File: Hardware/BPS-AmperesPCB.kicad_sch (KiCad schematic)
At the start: 34 parts, among them IC1 INA241A5IDR, IC2 AMC1350DWVR, IC3 OPA396DCKR, J1 Scrut In, J2 Shunt Resistor, SW1 Scrut Select, U1 TLV6001DCK

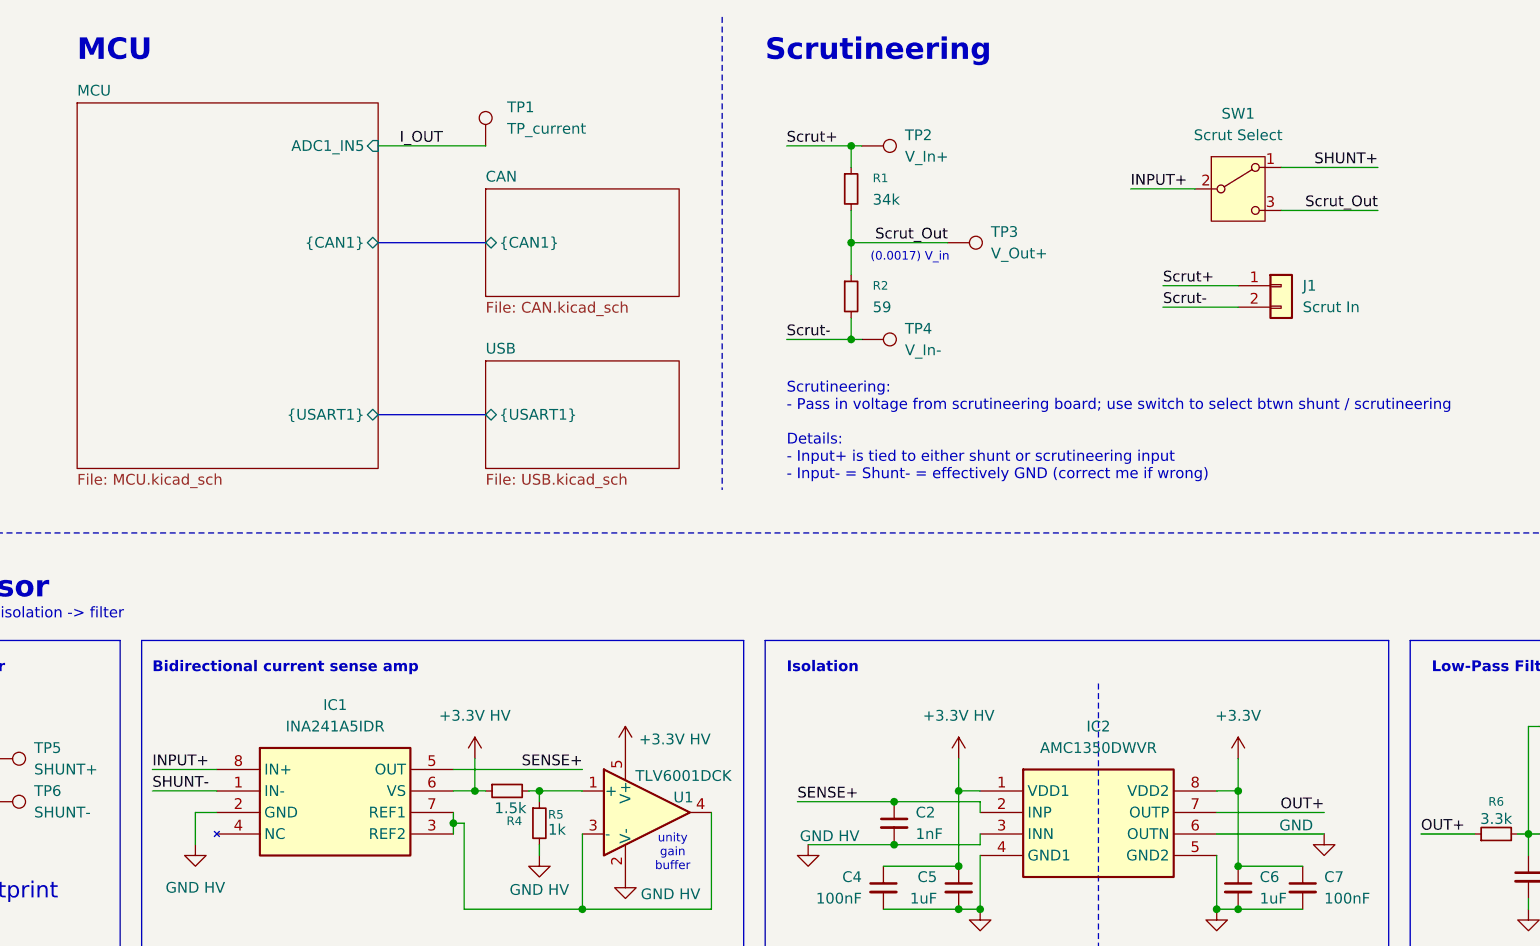
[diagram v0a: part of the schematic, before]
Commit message: dpdt switch for scrutineering
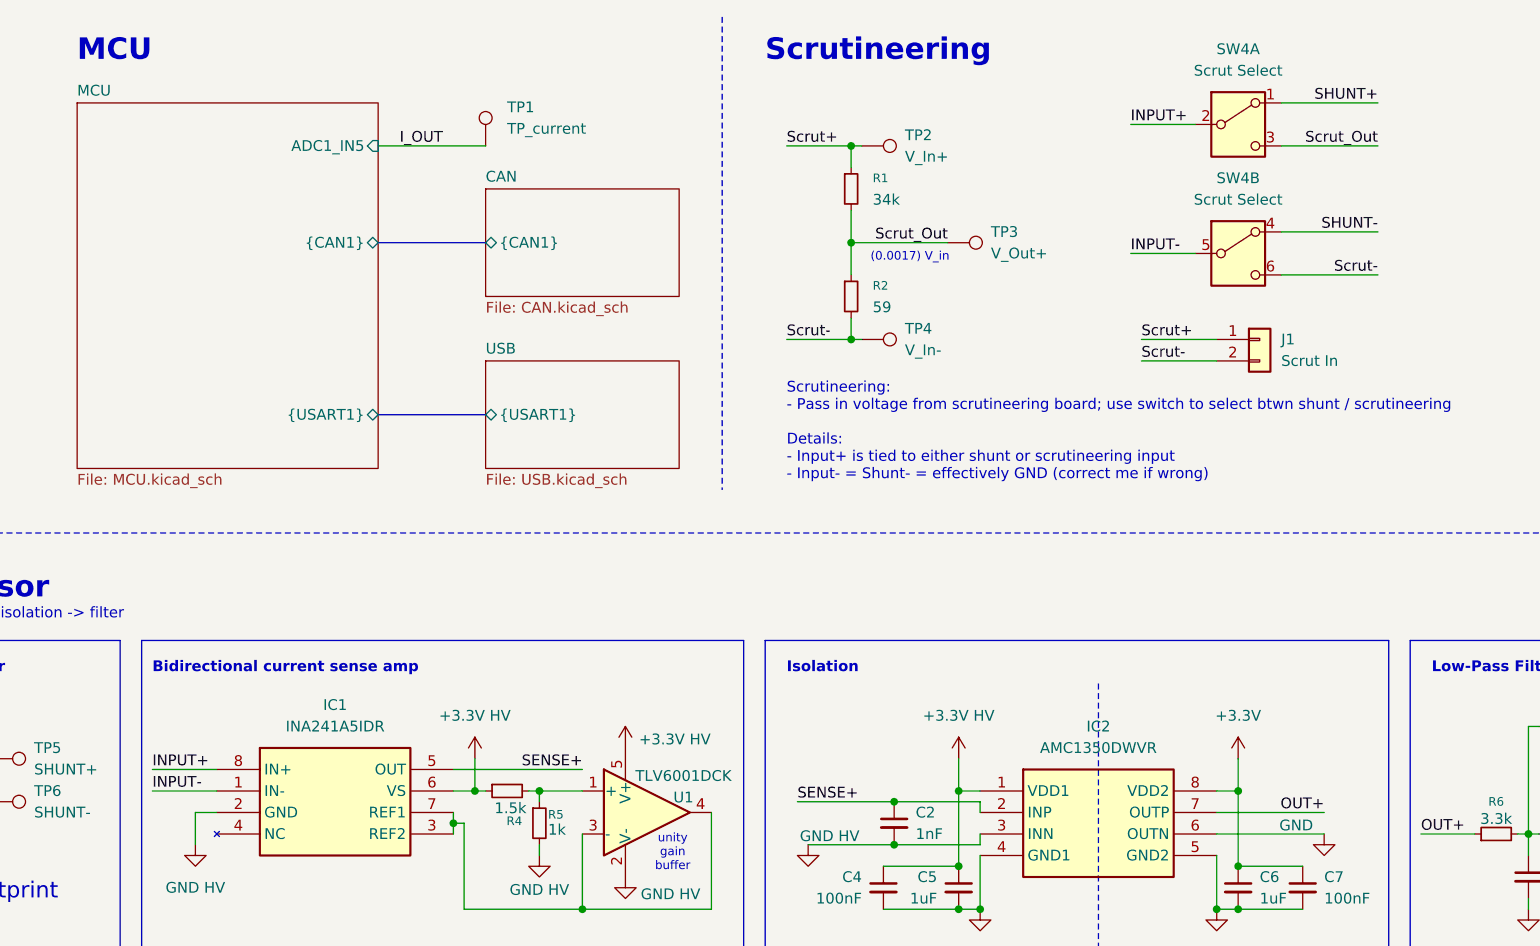
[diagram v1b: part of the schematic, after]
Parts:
- removed SW1: Scrut Select, symbol Switch:SW_SPDT
- added SW4: Scrut Select, symbol Switch:SW_DPDT_x2
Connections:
- net INPUT+: now also SW4.2 (B)
- net SHUNT+: now also SW4.1 (A)
- net SHUNT-: now also SW4.4 (A); no longer IC1.1 (IN-)
- net Scrut-: now also SW4.6 (C)
- net Scrut_Out: now also SW4.3 (C)
- new net INPUT-: IC1.1 (IN-), SW4.5 (B)
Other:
- moved on the sheet: J1

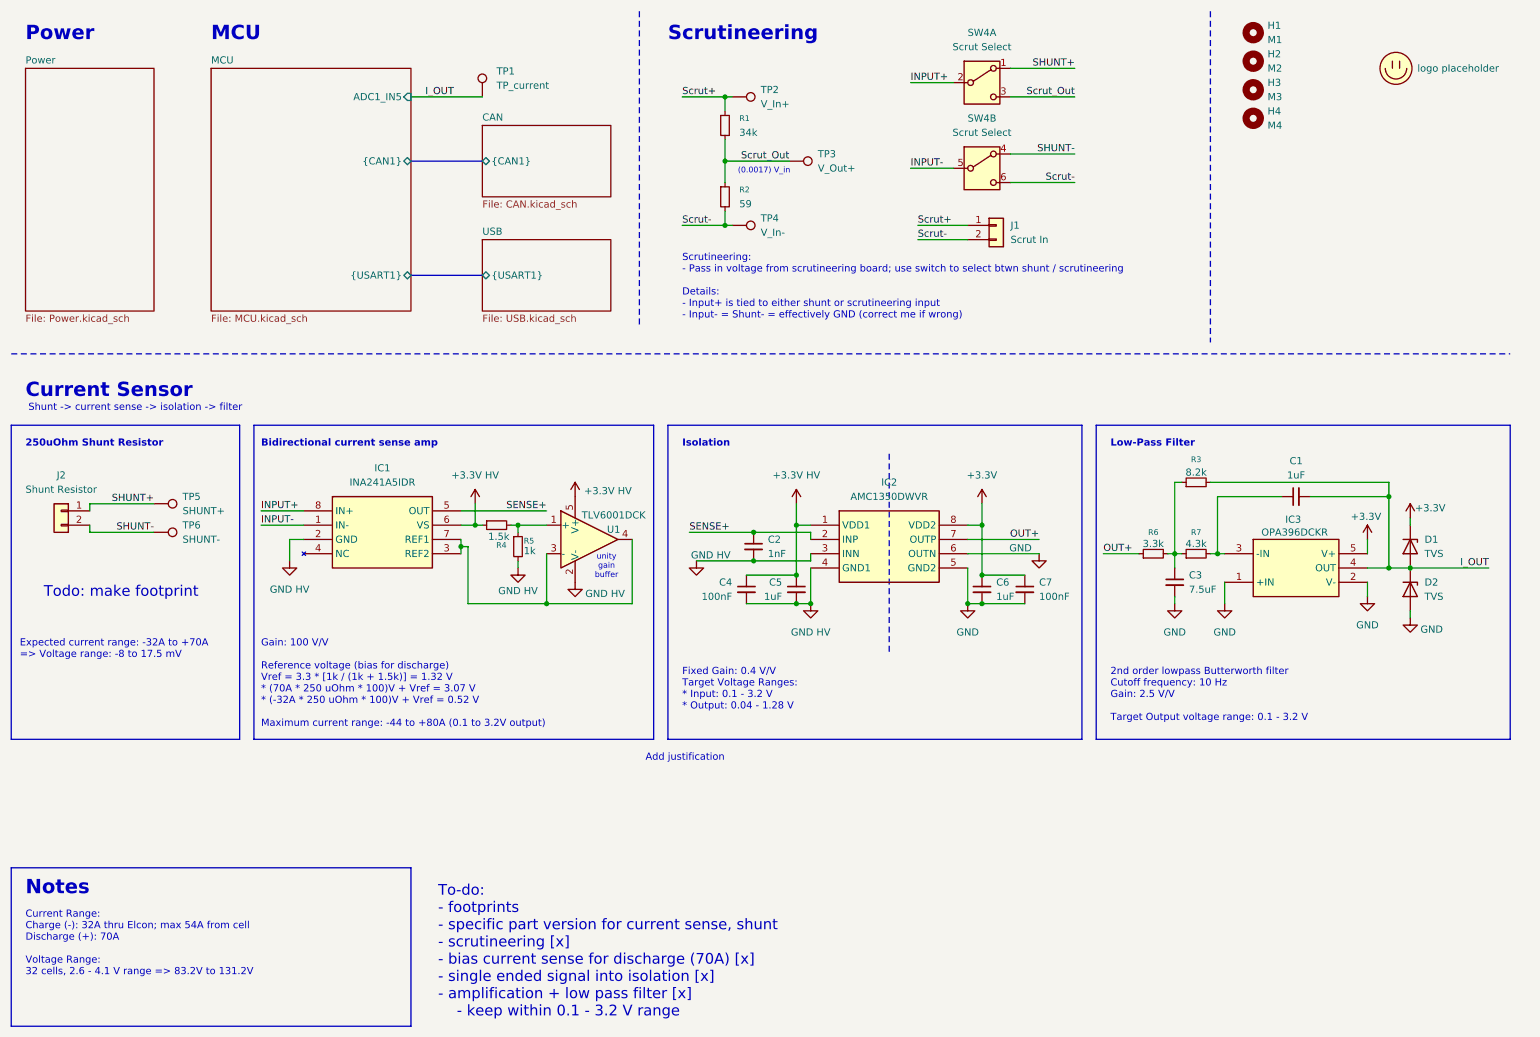
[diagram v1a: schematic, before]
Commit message: 24-5 buck from psom, OR gate for bootload. more sheet organization
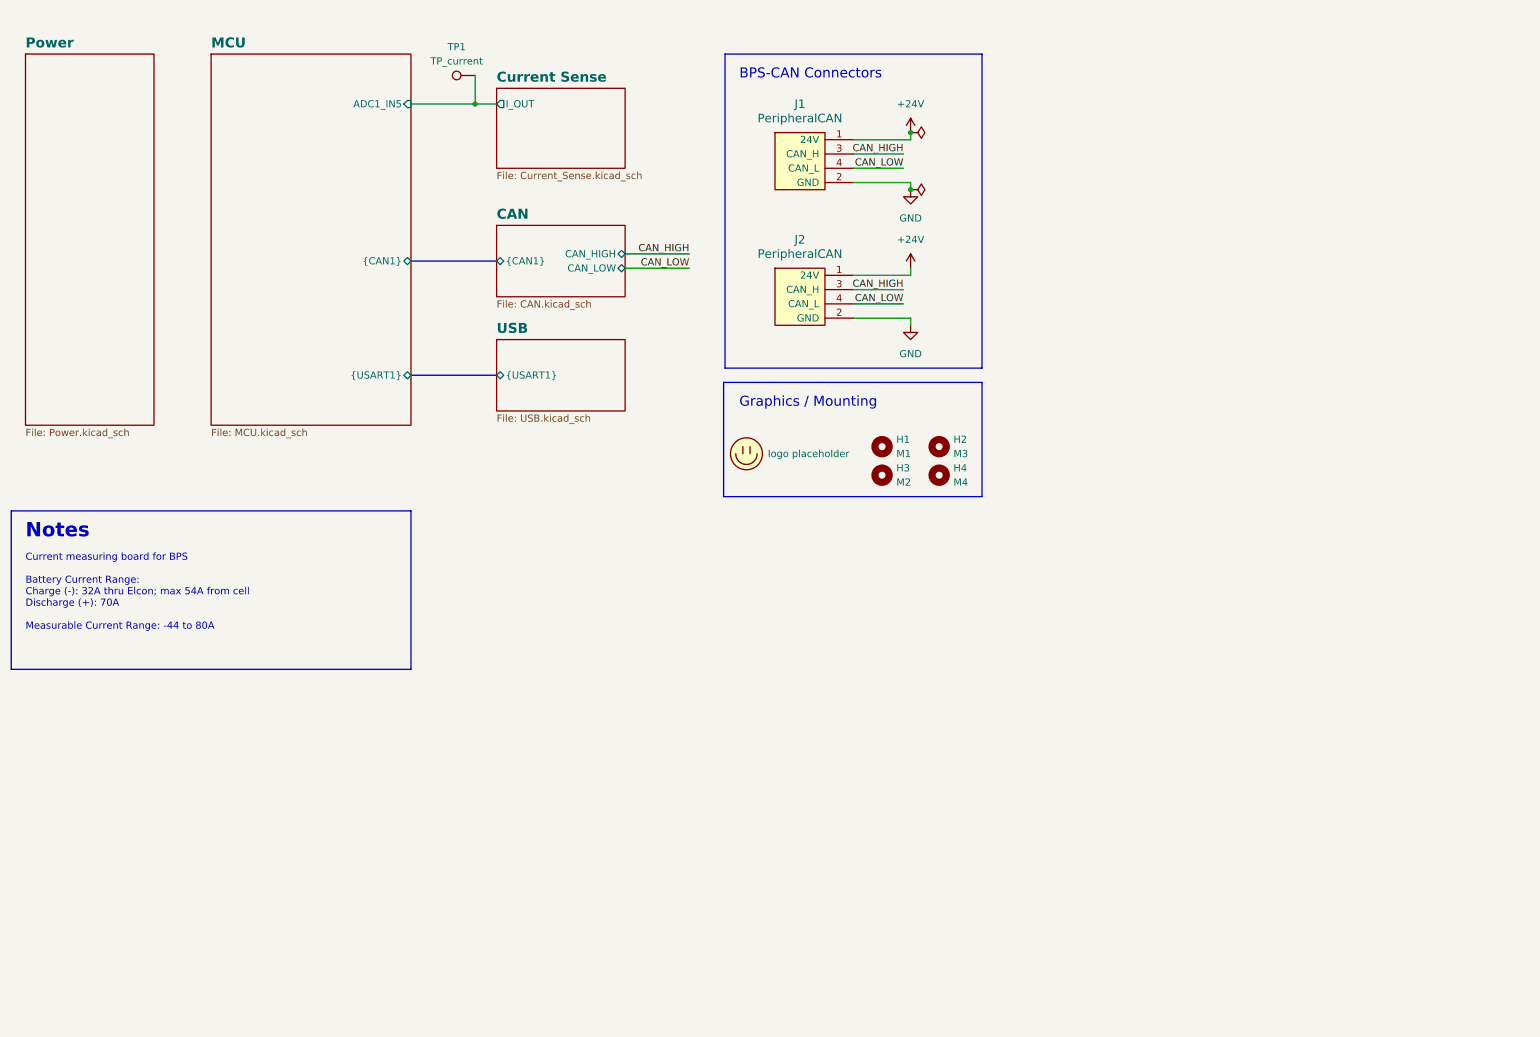
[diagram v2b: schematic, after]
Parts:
- removed C1, C5, C6: 1uF, Capacitor_SMD:C_0603_1608Metric_Pad1.08x0.95mm_HandSolder, symbol Device:C_Small
- removed C2: 1nF, Capacitor_SMD:C_0603_1608Metric_Pad1.08x0.95mm_HandSolder, symbol Device:C_Small
- removed C3: 7.5uF, Capacitor_SMD:C_0603_1608Metric_Pad1.08x0.95mm_HandSolder, symbol Device:C_Small
- removed C4, C7: 100nF, Capacitor_SMD:C_0603_1608Metric_Pad1.08x0.95mm_HandSolder, symbol Device:C_Small
- removed D1, D2: TVS, Diode_SMD:D_SOD-123F, symbol Device:D_Zener
- removed IC1: INA241A5IDR, SOIC127P600X175-8N, symbol INA241:INA241A5IDR
- removed IC2: AMC1350DWVR, Parts:AMC1350DWVR, symbol AMC1350:AMC1350DWVR
- removed IC3: OPA396DCKR, Parts:SOT65P210X110-5N, symbol OPA396DCKR:OPA396DCKR
- removed J1: Scrut In, Connector_Molex:Molex_Micro-Fit_3.0_43650-0200_1x02_P3.00mm_Horizontal, symbol Connector_Generic:Conn_01x02
- removed J2: Shunt Resistor, symbol Connector_Generic:Conn_01x02
- removed R1: 34k, Resistor_SMD:R_0603_1608Metric_Pad0.98x0.95mm_HandSolder, symbol Device:R_Small
- removed R2: 59, Resistor_SMD:R_0603_1608Metric_Pad0.98x0.95mm_HandSolder, symbol Device:R_Small
- removed R3: 8.2k, Resistor_SMD:R_0603_1608Metric_Pad0.98x0.95mm_HandSolder, symbol Device:R_Small
- removed R4: 1.5k, Resistor_SMD:R_0603_1608Metric_Pad0.98x0.95mm_HandSolder, symbol Device:R_Small
- removed R5: 1k, Resistor_SMD:R_0603_1608Metric_Pad0.98x0.95mm_HandSolder, symbol Device:R_Small
- removed R6: 3.3k, Resistor_SMD:R_0603_1608Metric_Pad0.98x0.95mm_HandSolder, symbol Device:R_Small
- removed R7: 4.3k, Resistor_SMD:R_0603_1608Metric_Pad0.98x0.95mm_HandSolder, symbol Device:R_Small
- removed SW4: Scrut Select, symbol Switch:SW_DPDT_x2
- removed TP2: V_In+, symbol Connector:TestPoint
- removed TP3: V_Out+, symbol Connector:TestPoint
- removed TP4: V_In-, symbol Connector:TestPoint
- removed TP5: SHUNT+, symbol Connector:TestPoint
- removed TP6: SHUNT-, symbol Connector:TestPoint
- removed U1: TLV6001DCK, Package_TO_SOT_SMD:SOT-353_SC-70-5, symbol Amplifier_Operational:TLV6001DCK
- added J1, J2: PeripheralCAN, UTSVT_Connectors:Molex_Nano-Fit_105309-xx04_1x04_P2.50mm_Vertical, symbol utsvt-connectors:PeripheralCANConnector
- renumbered H3 to H2, H2 to H3
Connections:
- net GND: now also J1.2 (GND), J2.2 (GND)
- net I_OUT renamed Current Sense/I_OUT
- new net +24V: J1.1 (24V), J2.1 (24V)
- new net CAN_HIGH: J1.3 (CAN_H), J2.3 (CAN_H)
- new net CAN_LOW: J1.4 (CAN_L), J2.4 (CAN_L)
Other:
- added sheet Current Sense (Current_Sense.kicad_sch)
- sheet CAN ports: added CAN_HIGH, CAN_LOW; removed none
- note added: "BPS-CAN Connectors"
- note added: "Current measuring board for BPS Battery Current Range: Charge (-): 32A thru Elcon; max 54A from cell Discharge (+): 70A Measurable Current Range: -44 to 80A"
- note added: "Graphics / Mounting"
- note removed: "(0.0017) V_in"
- note removed: "250uOhm Shunt Resistor"
- note removed: "2nd order lowpass Butterworth filter Cutoff frequency: 10 Hz Gain: 2.5 V/V Target Output voltage range: 0.1 - 3.2 V"
- note removed: "Add justification"
- note removed: "Bidirectional current sense amp"
- note removed: "Current Range: Charge (-): 32A thru Elcon; max 54A from cell Discharge (+): 70A Voltage Range: 32 cells, 2.6 - 4.1 V range => 83.2V to 131.2V"
- note removed: "Current Sensor"
- note removed: "Expected current range: -32A to +70A => Voltage range: -8 to 17.5 mV"
- note removed: "Fixed Gain: 0.4 V/V Target Voltage Ranges: * Input: 0.1 - 3.2 V * Output: 0.04 - 1.28 V"
- note removed: "Gain: 100 V/V Reference voltage (bias for discharge) Vref = 3.3 * [1k / (1k + 1.5k)] = 1.32 V * (70A * 250 uOhm * 100)V + Vref = 3.07 V * (-32A * 250 uOhm * 100)V + Vref = 0.52 V Maximum current range: -44 to +80A (0.1 to 3.2V output)"
- note removed: "Isolation"
- note removed: "Low-Pass Filter"
- note removed: "MCU"
- note removed: "Power"
- note removed: "Scrutineering"
- note removed: "Scrutineering: - Pass in voltage from scrutineering board; use switch to select btwn shunt / scrutineering Details: - Input+ is tied to either shunt or scrutineering input - Input- = Shunt- = effectively GND (correct me if wrong)"
- note removed: "Shunt -> current sense -> isolation -> filter"
- note removed: "To-do: - footprints - specific part version for current sense, shunt - scrutineering [x] - bias current sense for discharge (70A) [x] - single ended signal into isolation [x] - amplification + low pass filter [x] - keep within 0.1 - 3.2 V range"
- note removed: "Todo: make footprint"
- note removed: "unity gain buffer"
- moved on the sheet: H1, H2, H3, H4, TP1
